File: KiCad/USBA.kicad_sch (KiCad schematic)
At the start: 17 parts, among them J1 USB_A, SW1 SW_Push, U1 ESP32-WROOM-32, U2 FT231XQ, U3 LMR16006YQ3, U4 QR

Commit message: Kicad 6
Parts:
- U1: footprint RevK:ESP32-WROOM-32 -> RF_Module:ESP32-WROOM-32
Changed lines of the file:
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@@
   (title_block
     (title "Generic ESP32 USB-A")
-    (date "2021-11-06")
+    (date "${DATE}")
     (rev "1")
     (comment 1 "@TheRealRevK")
@@
     (property "Reference" "U1" (id 0) (at 65.405 27.1526 0))
     (property "Value" "ESP32-WROOM-32" (id 1) (at 65.405 29.464 0))
-    (property "Footprint" "RevK:ESP32-WROOM-32" (id 2) (at 65.405 105.41 0)
+    (property "Footprint" "RF_Module:ESP32-WROOM-32" (id 2) (at 65.405 105.41 0)
       (effects (font (size 1.27 1.27)) hide)
     )
@@
       (effects (font (size 1.27 1.27)) hide)
     )
-    (property "Datasheet" "https://www.mouser.co.uk/datasheet/2/216/APTF1616LSEEZGKQBKC-786442.pdf" (id 3) (at 74.295 124.46 0)
+    (property "Datasheet" "~" (id 3) (at 74.295 124.46 0)
       (effects (font (size 1.27 1.27)) hide)
     )
@@
       (effects (font (size 1.27 1.27)) (justify left))
     )
-    (property "Value" "LMR16006YQ3" (id 1) (at 178.435 56.515 0)
+    (property "Value" "LMR16006YQ3" (id 1) (at 180.975 56.515 0)
       (effects (font (size 1.27 1.27)) (justify left))
     )
@@
   (symbol (lib_id "RevK:Hidden") (at 193.675 46.355 0) (unit 1)
     (in_bom yes) (on_board yes)
-    (property "Reference" "C2" (id 0) (at 193.04 46.355 0)
+    (property "Reference" "C2" (id 0) (at 194.31 46.355 0)
       (effects (font (size 1.27 1.27)) (justify left))
     )
@@
       (effects (font (size 1.27 1.27)) hide)
     )
+    (property "Part No" "" (id 5) (at 193.675 46.355 0)
+      (effects (font (size 1.27 1.27)) hide)
+    )
     (pin "~")
   )
   (symbol (lib_id "RevK:Hidden") (at 193.675 48.26 0) (unit 1)
     (in_bom yes) (on_board yes)
-    (property "Reference" "C3" (id 0) (at 193.04 48.26 0)
+    (property "Reference" "C3" (id 0) (at 194.31 48.26 0)
       (effects (font (size 1.27 1.27)) (justify left))
     )
@@
       (effects (font (size 1.27 1.27)) hide)
     )
+    (property "Part No" "" (id 5) (at 193.675 48.26 0)
+      (effects (font (size 1.27 1.27)) hide)
+    )
     (pin "~")
   )
   (symbol (lib_id "RevK:Hidden") (at 193.675 50.165 0) (unit 1)
     (in_bom yes) (on_board yes)
-    (property "Reference" "C4" (id 0) (at 193.04 50.165 0)
+    (property "Reference" "C4" (id 0) (at 194.31 50.165 0)
       (effects (font (size 1.27 1.27)) (justify left))
     )
@@
       (effects (font (size 1.27 1.27)) hide)
     )
+    (property "Part No" "" (id 5) (at 193.675 50.165 0)
+      (effects (font (size 1.27 1.27)) hide)
+    )
     (pin "~")
   )
   (symbol (lib_id "RevK:Hidden") (at 193.675 52.07 0) (unit 1)
     (in_bom yes) (on_board yes)
-    (property "Reference" "L1" (id 0) (at 193.04 52.07 0)
+    (property "Reference" "L1" (id 0) (at 194.31 52.07 0)
       (effects (font (size 1.27 1.27)) (justify left))
     )
@@
       (effects (font (size 1.27 1.27)) hide)
     )
+    (property "Note" "" (id 6) (at 193.675 52.07 0)
+      (effects (font (size 1.27 1.27)) hide)
+    )
     (pin "~")
   )
   (symbol (lib_id "RevK:Hidden") (at 193.675 53.975 0) (unit 1)
     (in_bom yes) (on_board yes)
-    (property "Reference" "D2" (id 0) (at 193.04 53.975 0)
+    (property "Reference" "D2" (id 0) (at 194.31 53.975 0)
       (effects (font (size 1.27 1.27)) (justify left))
     )
@@
     )
     (property "Part No" "CD1206-B2100" (id 5) (at 193.675 53.975 0)
+      (effects (font (size 1.27 1.27)) hide)
+    )
+    (property "Note" "" (id 6) (at 193.675 53.975 0)
       (effects (font (size 1.27 1.27)) hide)
     )
@@
     )
     (path "/00000000-0000-0000-0000-00006043326c"
-      (reference "U1") (unit 1) (value "ESP32-WROOM-32") (footprint "RevK:ESP32-WROOM-32")
+      (reference "U1") (unit 1) (value "ESP32-WROOM-32") (footprint "RF_Module:ESP32-WROOM-32")
     )
     (path "/00000000-0000-0000-0000-000060849d1e"

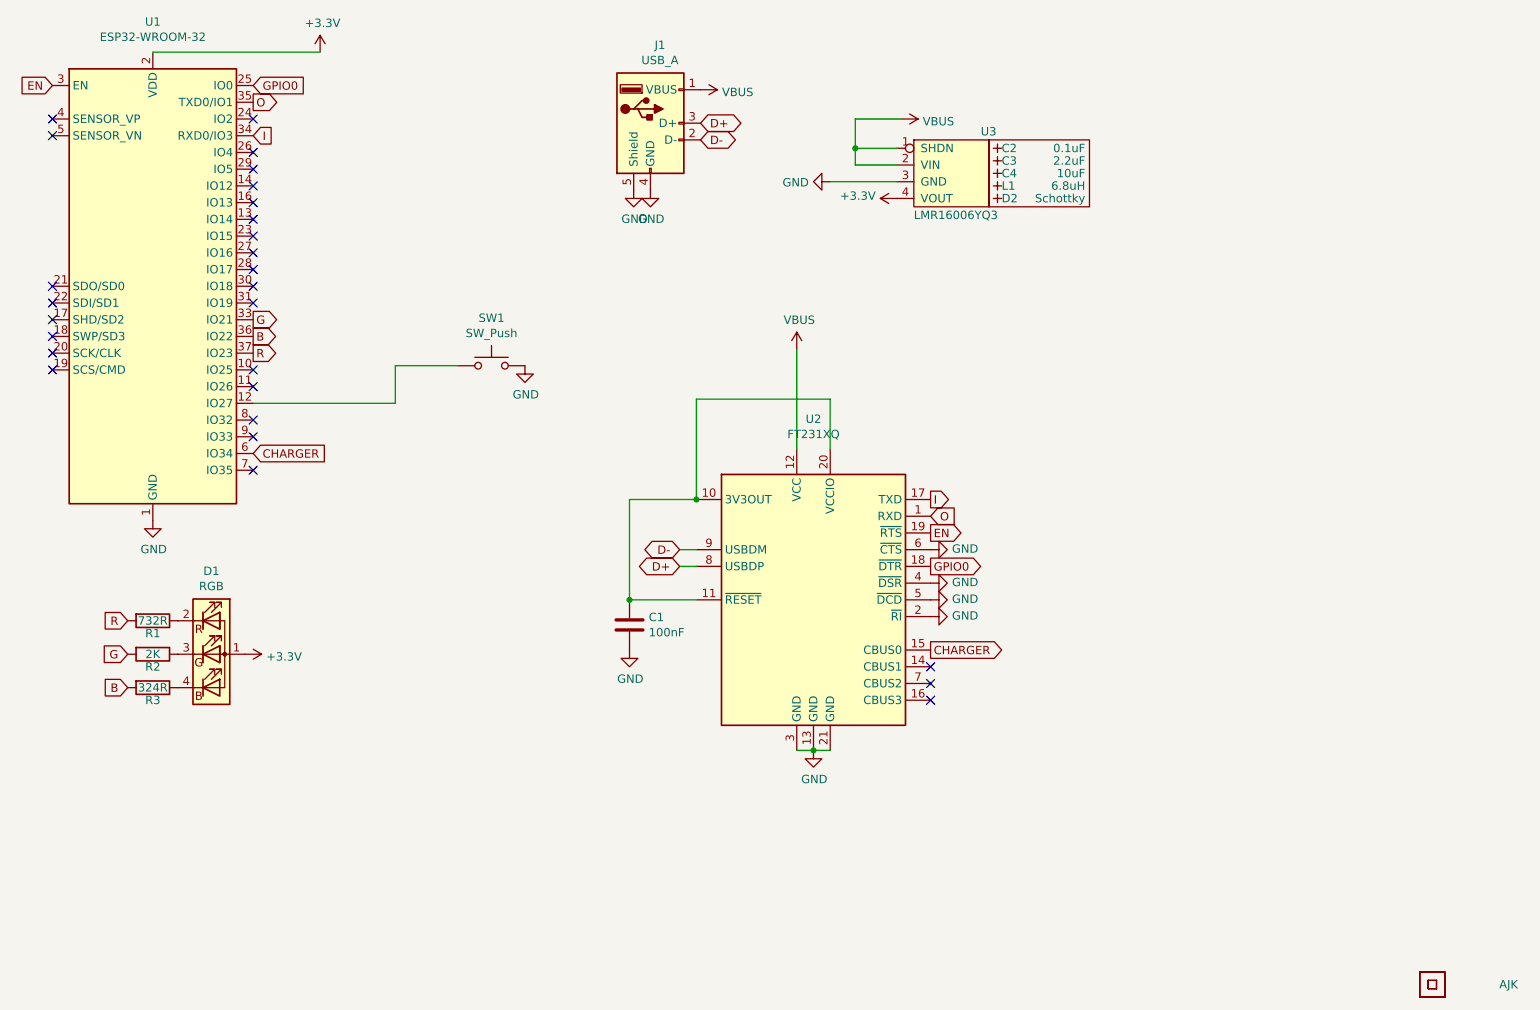
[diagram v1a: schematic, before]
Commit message: Lots of tidy - mainly silkscreen stuff
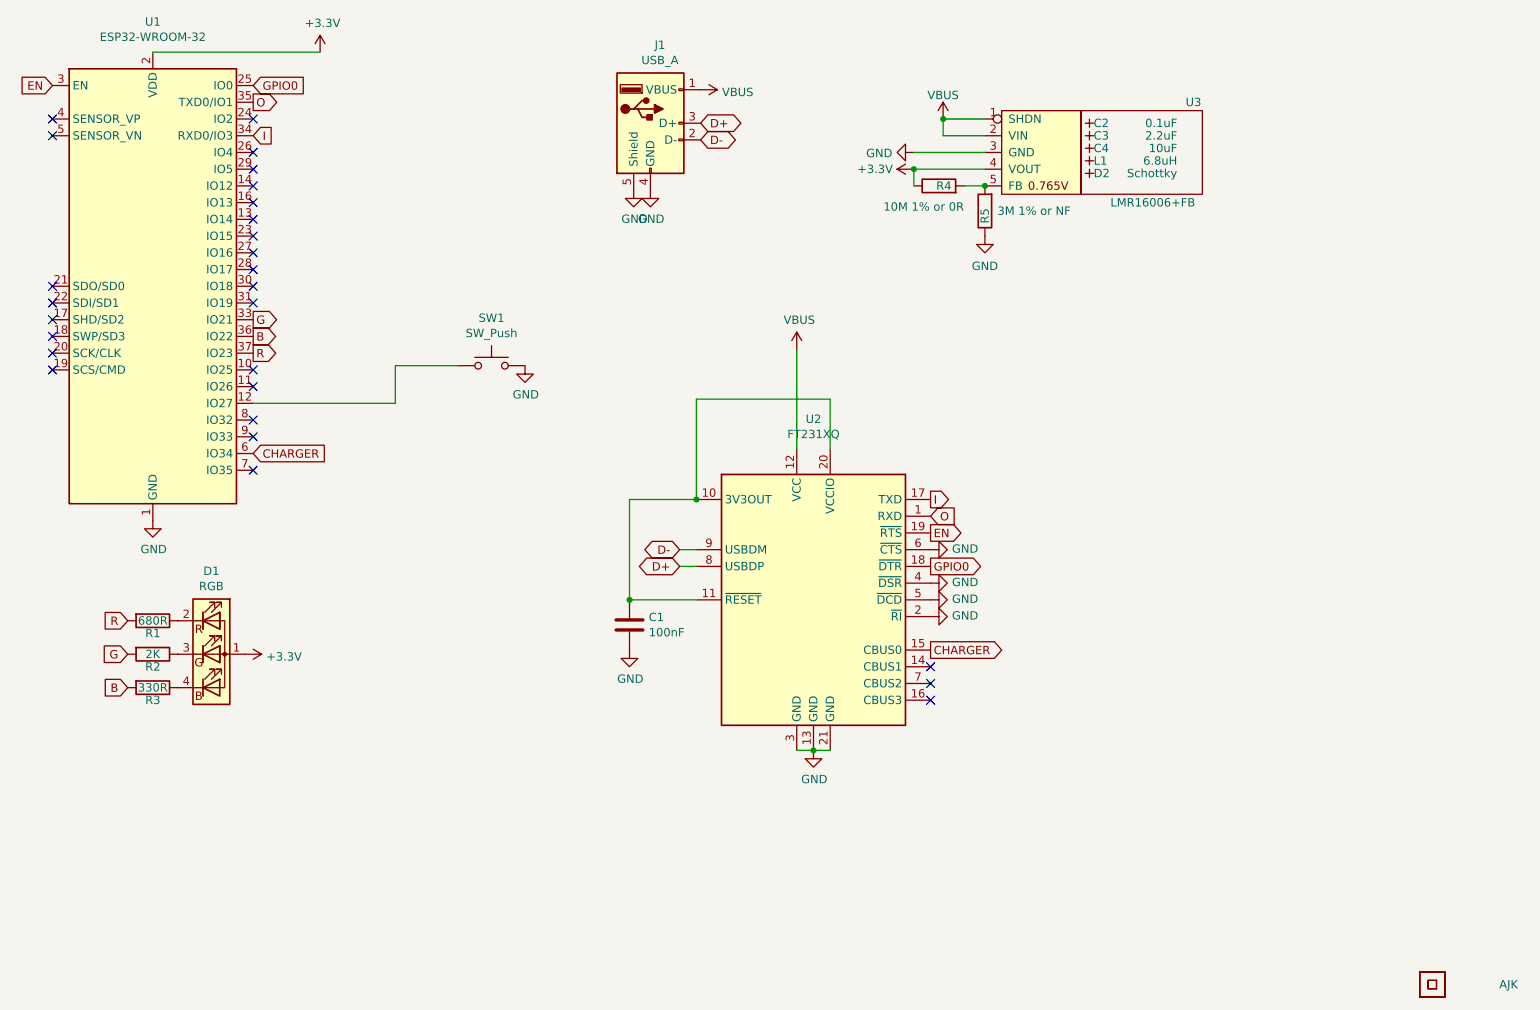
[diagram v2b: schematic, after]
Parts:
- removed U3: LMR16006YQ3, RevK:RegulatorBlock, symbol RevK:LMR16006YQ3
- added R4: 10M 1% or 0R, RevK:R_0603, symbol Device:R
- added R5: 3M 1% or NF, RevK:R_0603, symbol Device:R
- added U3: LMR16006+FB, RevK:RegulatorBlockFB, symbol RevK:LMR16006+FB
- R1: value 732R -> 680R
- R3: value 324R -> 330R
- U1: footprint RF_Module:ESP32-WROOM-32 -> RevK:ESP32-WROOM-32
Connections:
- net +3V3: now also R4.1, U3.4 (VOUT)
- net GND: now also R5.1, U3.3 (GND)
- net VBUS: now also U3.1 (SHDN), U3.2 (VIN)
- new net: R4.2, R5.2, U3.5 (FB)
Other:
- moved on the sheet: C2, C3, C4, D2, L1

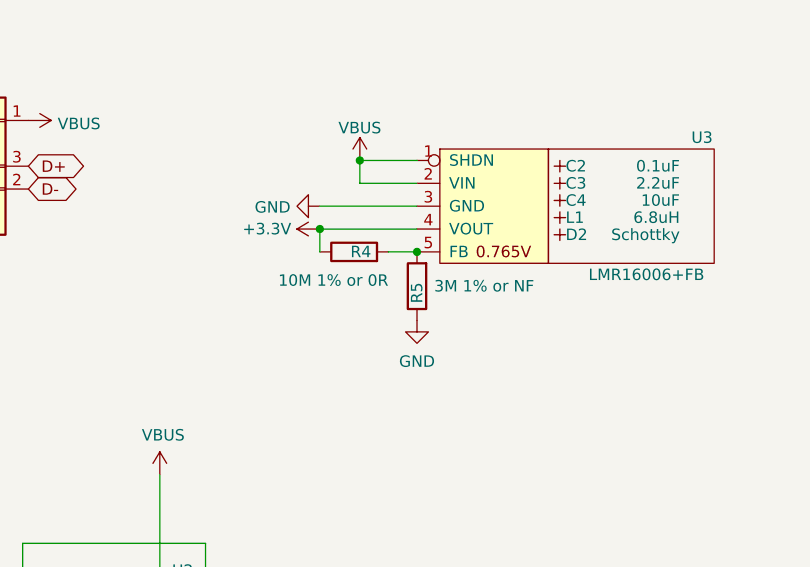
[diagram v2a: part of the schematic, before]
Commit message: Change resistor values
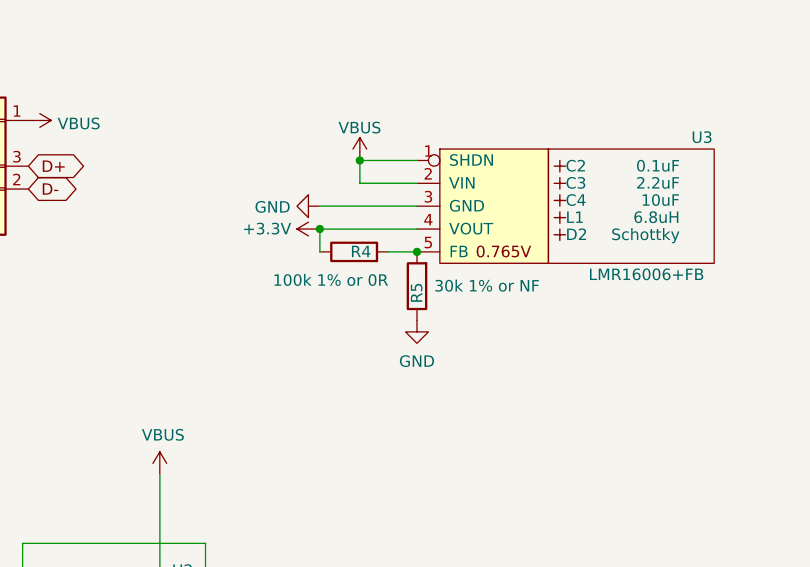
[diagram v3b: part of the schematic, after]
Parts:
- R4: value 10M 1% or 0R -> 100k 1% or 0R
- R5: value 3M 1% or NF -> 30k 1% or NF
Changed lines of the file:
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@@
       (effects (font (size 1.27 1.27)) (justify left))
     )
-    (property "Value" "10M 1% or 0R" (id 1) (at 188.595 55.245 90)
+    (property "Value" "100k 1% or 0R" (id 1) (at 188.595 55.245 90)
       (effects (font (size 1.27 1.27)) (justify left))
     )
@@
       (effects (font (size 1.27 1.27)) (justify right))
     )
-    (property "Value" "3M 1% or NF" (id 1) (at 193.675 55.88 0)
+    (property "Value" "30k 1% or NF" (id 1) (at 193.675 55.88 0)
       (effects (font (size 1.27 1.27)) (justify right))
     )
@@
     )
     (path "/0822ca37-715d-4e56-a8e3-be77335446d8"
-      (reference "R4") (unit 1) (value "10M 1% or 0R") (footprint "RevK:R_0603")
+      (reference "R4") (unit 1) (value "100k 1% or 0R") (footprint "RevK:R_0603")
     )
     (path "/e06620f1-6613-429a-ab9d-1435eff32a58"
-      (reference "R5") (unit 1) (value "3M 1% or NF") (footprint "RevK:R_0603")
+      (reference "R5") (unit 1) (value "30k 1% or NF") (footprint "RevK:R_0603")
     )
     (path "/00000000-0000-0000-0000-0000618d0b84"

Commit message: Library update
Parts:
- removed C1: 100nF, RevK:C_0603, symbol Device:C
- removed C4: 10uF, RevK:Hidden, symbol RevK:Hidden
- removed Logo1: AJK, RevK:AJK, symbol RevK:AJK
- removed SW1: SW_Push, RevK:SW_PUSH_6mm_SMD, symbol Switch:SW_Push
- removed U1: ESP32-WROOM-32, RevK:ESP32-WROOM-32, symbol RF_Module:ESP32-WROOM-32
- removed U2: FT231XQ, RevK:QFN-20-1EP_4x4mm_P0.5mm_EP2.5x2.5mm, symbol Interface_USB:FT231XQ
- removed U3: LMR16006+FB, RevK:RegulatorBlockFB, symbol RevK:LMR16006+FB
- added C1: 0.1uF, RevK:C_0603_, symbol RevK:Hidden
- added C4: 100nF, RevK:C_0603, symbol Device:C
- added J2: Shelly, RevK:Shelly, symbol RevK:Shelly
- added R6: 10k, symbol Device:R
- added U1: ESP32-PICO-MINI-02, RevK:ESP32-PICO-MINI-02, symbol RevK:ESP32-PICO-MINI-02
- added U2: LMR16006+FB, RevK:SOT-23-Thin-6-Reg, symbol RevK:LMR16006+FB
- C2: value 0.1uF -> 2.2uF; footprint RevK:Hidden -> RevK:C_0805_; Note X7R or X5R 0603 -> 0603 or 0805; Part No (none) -> 0805-2.2uF-25V
- C3: value 2.2uF -> 10uF; footprint RevK:Hidden -> RevK:C_0805_; Part No (none) -> 0805-10uF-16V
- D2: footprint RevK:Hidden -> RevK:D_1206_
- L1: footprint RevK:Hidden -> RevK:L_4x4_; Part No TYA4020 -> TYA40206R8M-10
- R4: Part No (none) -> 0603-100k
- R5: Part No (none) -> 0603-30k
- U4: footprint RevK:QR-HA -> RevK:QR-GENERIC; Note (none) -> Non part, PCB printed
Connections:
- net B: now also U1.33 (IO19)
- net CHARGER: now also U1.34 (IO22)
- net EN: now also R6.2, U1.8 (EN)
- net G: now also U1.26 (IO20)
- net GND: now also C4.2, J2.1 (GND), U1.1 (GND), U1.11 (GND), U1.14 (GND), U1.2 (GND), U1.36 (GND), U1.37 (GND), U1.38 (GND), U1.39 (GND), U1.40 (GND), U1.41 (GND), U1.42 (GND), U1.43 (GND), U1.44 (GND), U1.45 (GND), U1.46 (GND), U1.47 (GND), U1.48 (GND), U1.49 (GND), U1.50 (GND), U1.51 (GND), U1.52 (GND), U1.53 (GND), U2.3 (GND)
- net GPIO0: now also J2.2 (0), U1.23 (IO0)
- net I: now also J2.4 (Rx), U1.30 (RXD0)
- net O: now also J2.5 (Tx), U1.31 (TXD0)
- net R: now also U1.35 (IO21)
- net VBUS: now also U2.1 (SHDN), U2.2 (VIN)
- net at R4.2, R5.2: now also U2.5 (FB)
- net +3V3 renamed +3.3V
- net +3.3V: now also C4.1, J2.3 (3V3), R6.1, U1.3 (3V3), U2.4 (VOUT)
- net D+: no longer names the net of J1.3 (D+)
- net D-: no longer names the net of J1.2 (D-)
- no-connect marks 27 -> 22
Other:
- note added: "User either variable LMR16006 with 100k/30k Or fixed 3.3V LMR16006 Q3 part with 0R/NF"
- moved on the sheet: D1, J1, R1, R2, R3
